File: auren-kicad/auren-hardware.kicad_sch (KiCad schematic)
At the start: 10 parts, among them J1 USB_B_Mini, J2 USB_B_Mini, J3 Speaker_1, J4 Speaker_2, J5 Speaker_1, J6 Speaker_2

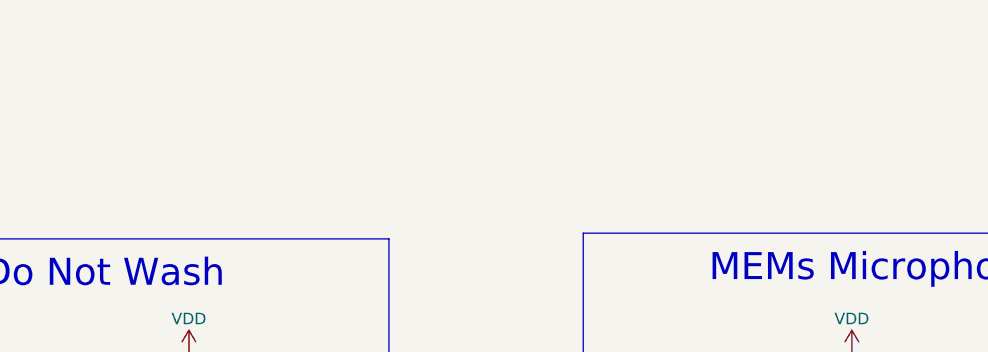
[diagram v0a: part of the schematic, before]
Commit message: Added schematic pdf
Cleaned up the files. Ready for v1.0 release
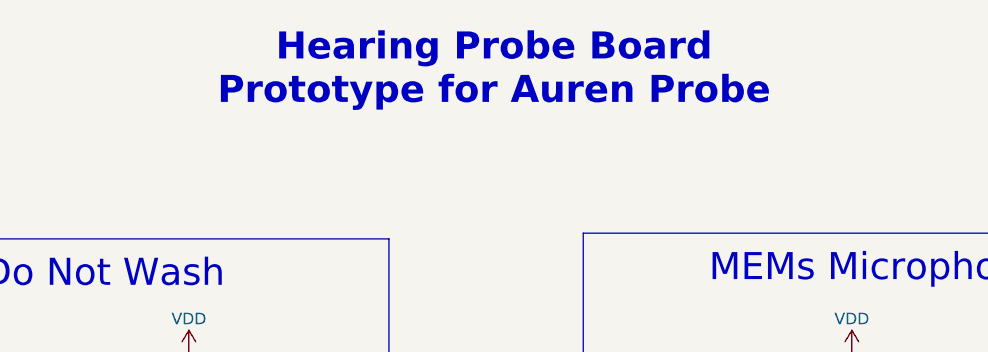
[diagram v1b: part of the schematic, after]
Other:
- note added: "Hearing Probe Board Prototype for Auren Probe"
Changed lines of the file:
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@@
 	(title_block
 		(title "Hearing Probe Board")
-		(rev "v0.1")
+		(date "2025-08-28")
+		(rev "v1.0")
 		(company "Flywheel Lab")
 		(comment 1 "Desiged for Creare")
@@
 		)
 	)
+	(text "Hearing Probe Board\nPrototype for Auren Probe"
+		(exclude_from_sim no)
+		(at 133.604 29.21 0)
+		(effects
+			(font
+				(size 3 3)
+				(thickness 0.6)
+				(bold yes)
+			)
+			(justify bottom)
+		)
+	)

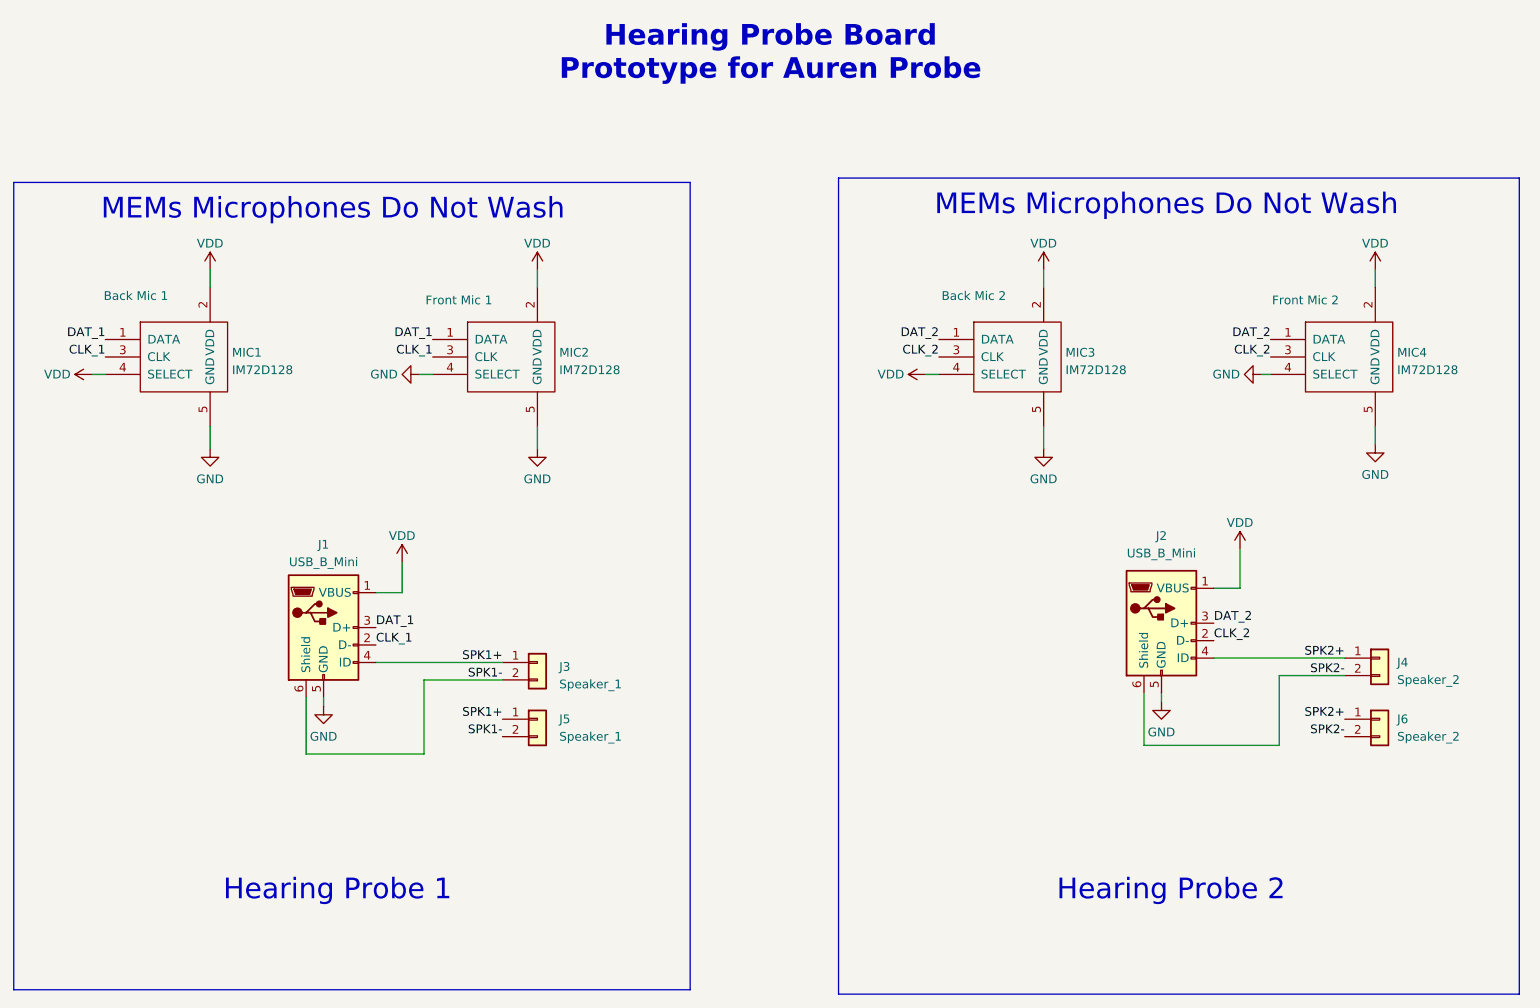
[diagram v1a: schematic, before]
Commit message: Added outline shape files
Imported DXF to PCB layout file and converted to board outline.
Rough component placement
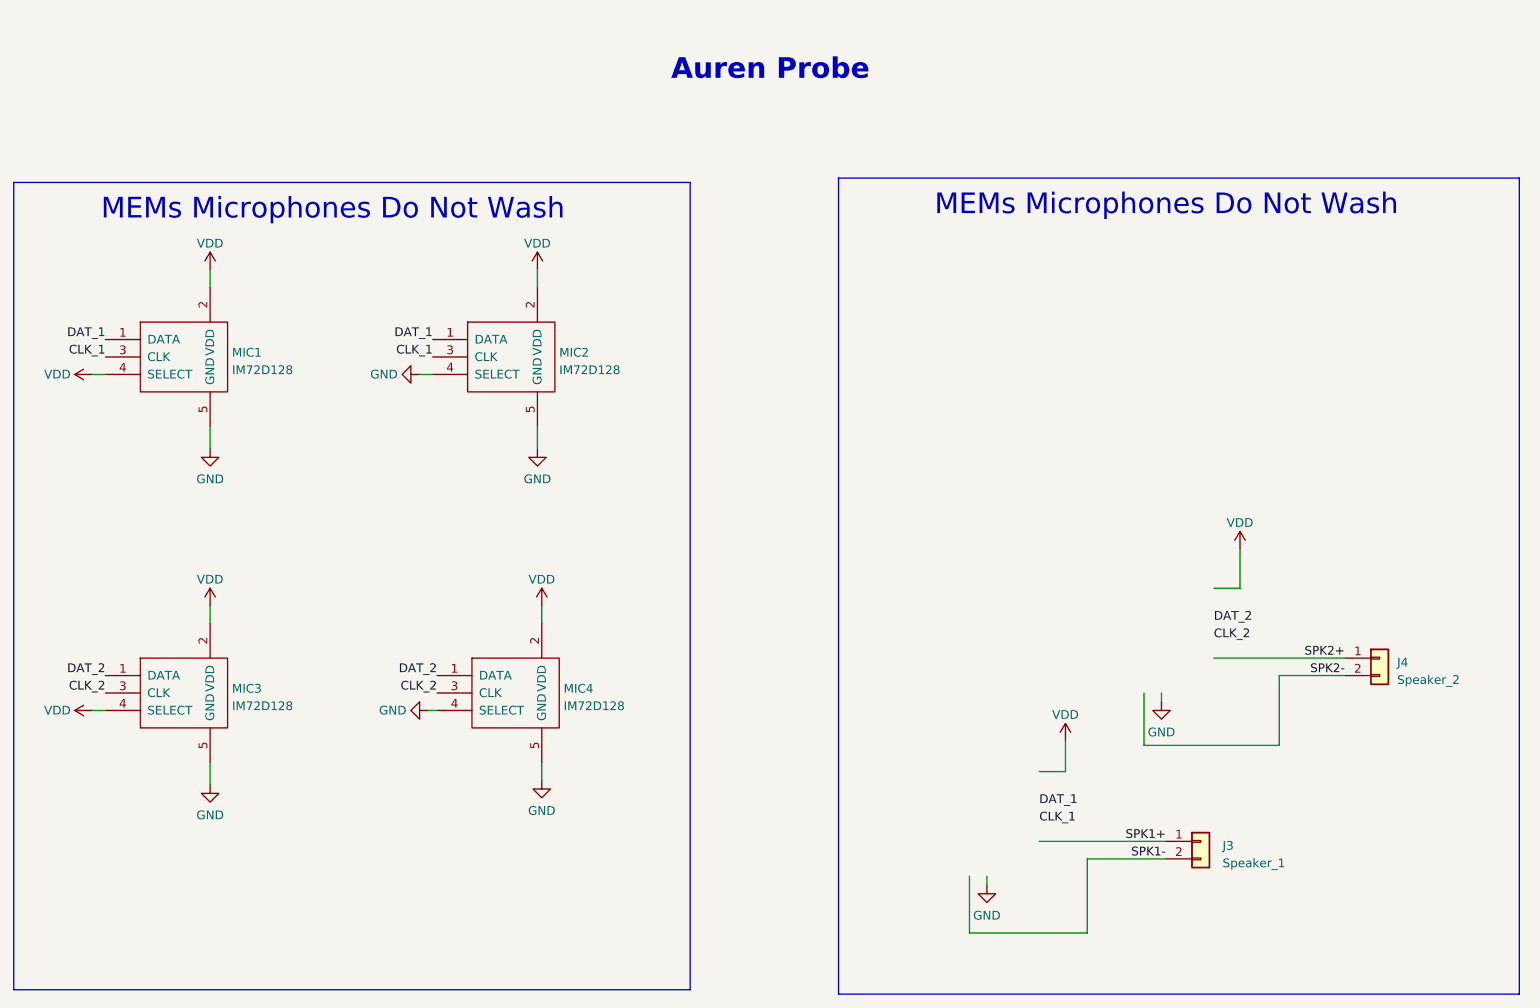
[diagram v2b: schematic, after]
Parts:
- removed J1, J2: USB_B_Mini, Flywheel:MOLEX_56579-0519, symbol Connector:USB_B_Mini
- removed J5: Speaker_1, Connector_PinHeader_2.00mm:PinHeader_1x02_P2.00mm_Vertical, symbol Connector_Generic:Conn_01x02
- removed J6: Speaker_2, Connector_PinHeader_2.00mm:PinHeader_1x02_P2.00mm_Vertical, symbol Connector_Generic:Conn_01x02
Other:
- note added: "Auren Probe"
- note removed: "Hearing Probe 1"
- note removed: "Hearing Probe 2"
- note removed: "Hearing Probe Board Prototype for Auren Probe"
- moved on the sheet: J3, MIC3, MIC4
